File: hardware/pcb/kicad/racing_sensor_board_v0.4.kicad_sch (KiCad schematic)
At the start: 53 parts, among them J0 TC0, J1 TC1, J10 NTC2, J11 NTC3, J12 OUT0, J13 OUT1, J14 OUT2, J15 OUT3, J16 ANA0, J17 ANA1, J18 ANA2, J19 ANA3, J2 TC2, J20 ANA4, J21 ANA5, J22 ANA6, J23 ANA7, J24 DIG0, J25 DIG1, J26 DIG2, J27 DIG3, J28 DIG4, J29 DIG5, J3 TC3, J30 PWR_IN, J4 TC4, J5 TC5, J6 TC6, J7 TC7, J8 NTC0, J9 NTC1, Q1 AO3400A, Q2 AO3400A, Q3 AO3400A, Q4 AO3400A, U1 Teensy_4.1, U10 MAX31855KASA+, U11 LIS3DH, U12 MP2307DN, U2 WIZ820io, U3 MAX31855KASA+, U4 MAX31855KASA+, U5 MAX31855KASA+, U6 MAX31855KASA+, U7 MAX31855KASA+, U8 MAX31855KASA+, U9 MAX31855KASA+

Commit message: Fix unterminated string in v0.4 schematic (MP2307DN note text)
https://claude.ai/code/session_01NVvsy3kMr9piDWfs5WdvpG
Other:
- note added: "Cout, Lout, R-divider — add manually in KiCad"
- note removed: "Cout, Lout, R-divider add manually in KiCad"
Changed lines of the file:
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@@
     (effects (font (size 1.27 1.27)))
  )
-  (text "Cout, Lout, R-divider
-add manually in KiCad" (at 332.00 321.35 0)
+  (text "Cout, Lout, R-divider — add manually in KiCad" (at 332.00 321.35 0)
     (effects (font (size 1.5 1.5)) (justify left))
  )

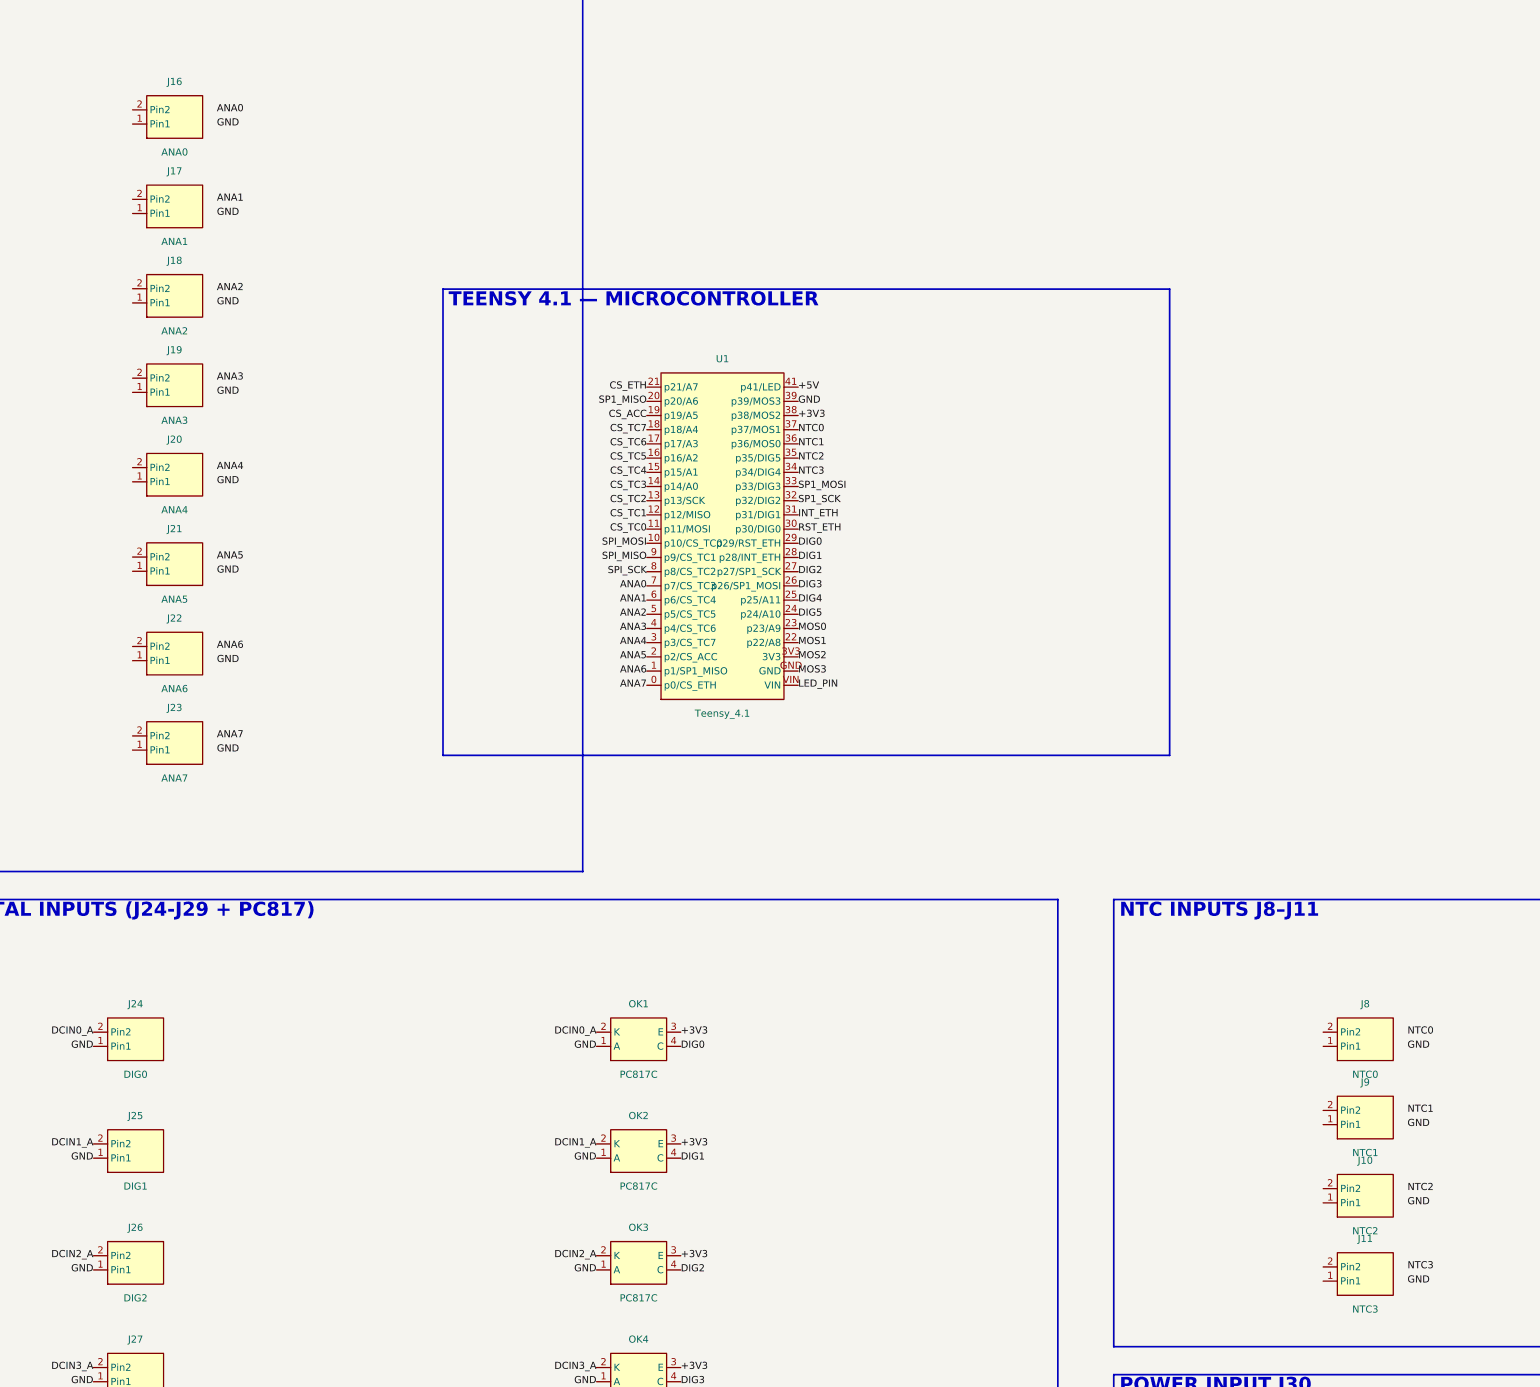
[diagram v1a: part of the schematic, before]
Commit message: Fix pin/label mismatch in v0.4 analog and NTC connector sections
J16-J23 and J8-J11 use Conn2pin which has left-side pins, but labels
were placed on the right side (rp_xy), causing 'Pin not connected' and
'Label not connected' ERC violations. Fixed to use lp_xy/llbl.

https://claude.ai/code/session_01NVvsy3kMr9piDWfs5WdvpG
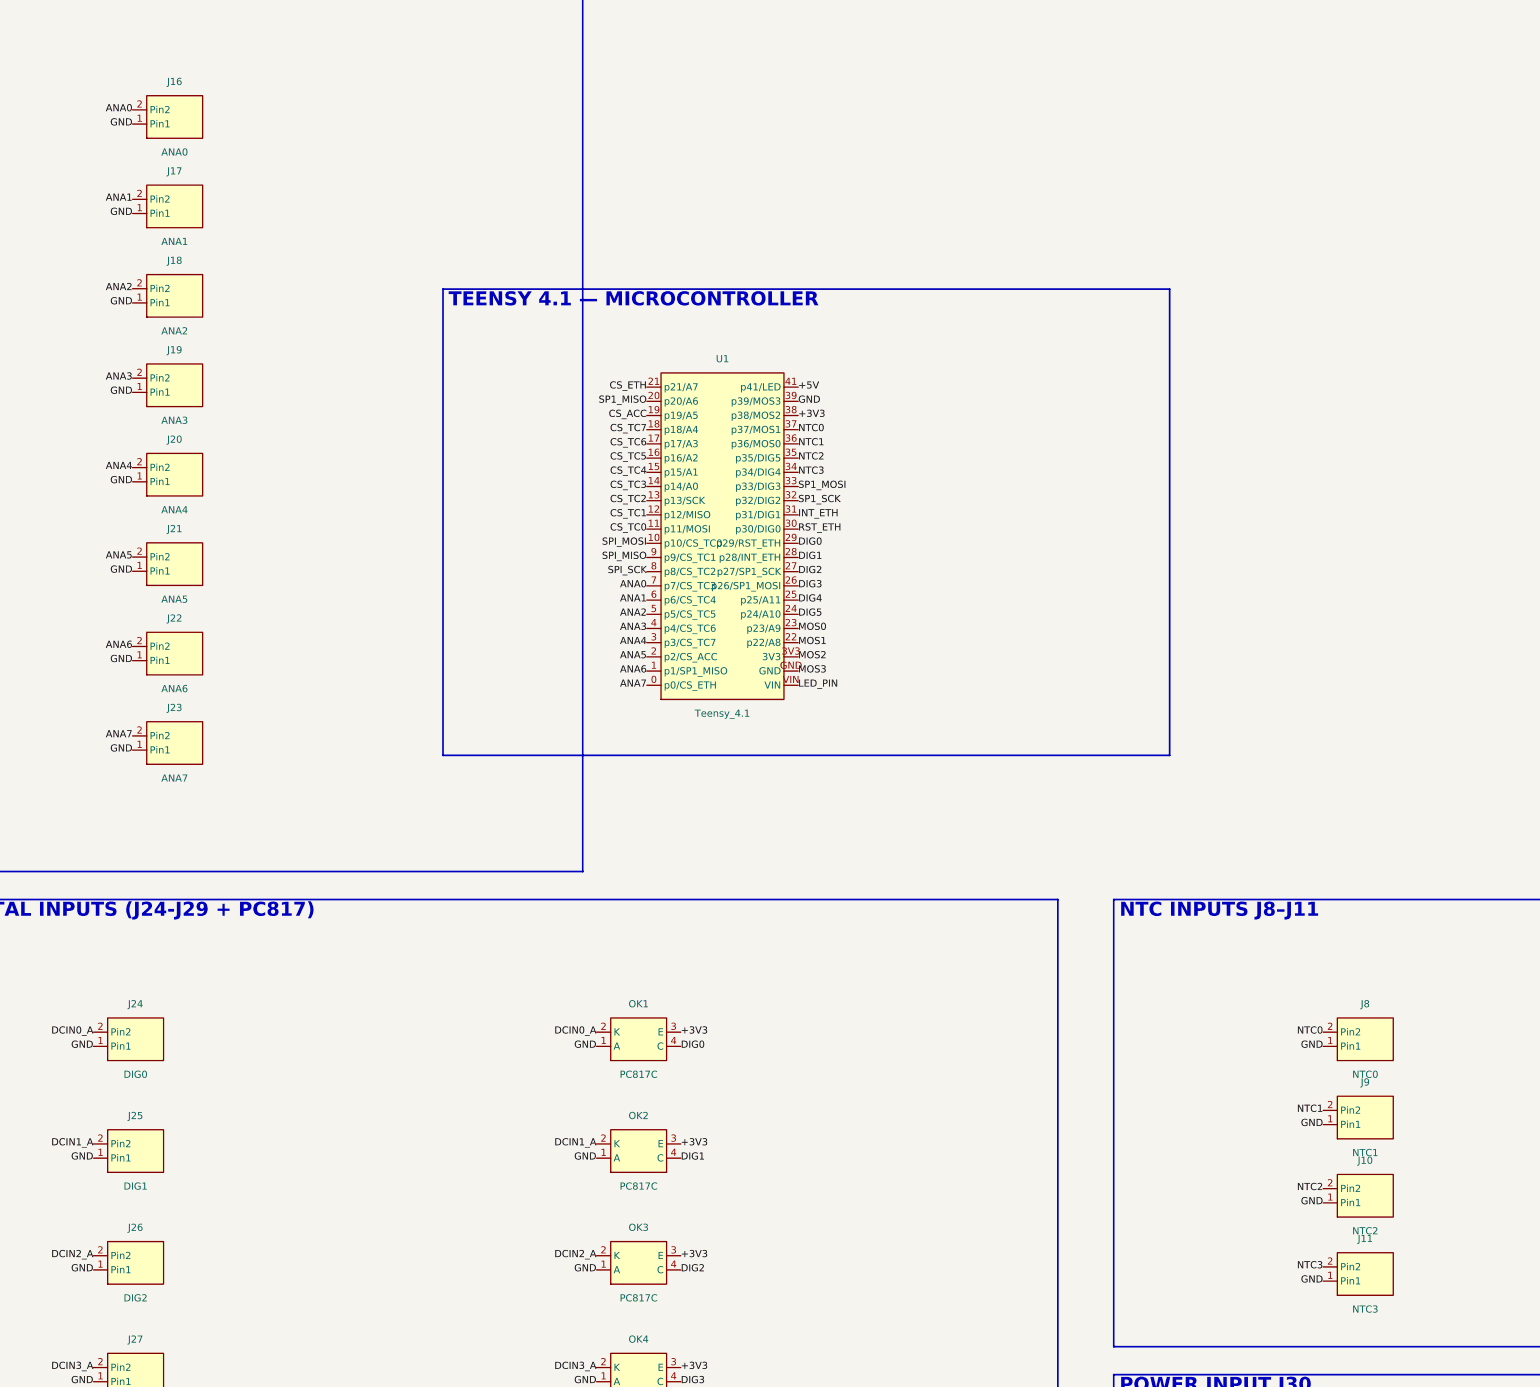
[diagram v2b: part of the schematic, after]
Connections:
- net ANA0: now also J16.2 (Pin2)
- net ANA1: now also J17.2 (Pin2)
- net ANA2: now also J18.2 (Pin2)
- net ANA3: now also J19.2 (Pin2)
- net ANA4: now also J20.2 (Pin2)
- net ANA5: now also J21.2 (Pin2)
- net ANA6: now also J22.2 (Pin2)
- net ANA7: now also J23.2 (Pin2)
- net GND: now also J10.1 (Pin1), J11.1 (Pin1), J16.1 (Pin1), J17.1 (Pin1), J18.1 (Pin1), J19.1 (Pin1), J20.1 (Pin1), J21.1 (Pin1), J22.1 (Pin1), J23.1 (Pin1), J8.1 (Pin1), J9.1 (Pin1)
- net NTC0: now also J8.2 (Pin2)
- net NTC1: now also J9.2 (Pin2)
- net NTC2: now also J10.2 (Pin2)
- net NTC3: now also J11.2 (Pin2)
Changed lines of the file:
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@@
     (pin "2")
   )
-  (label "ANA0" (at 79.54 153.73 0)
-    (effects (font (size 1.27 1.27)))
- )
-  (label "GND" (at 79.54 156.27 0)
+  (label "ANA0" (at 64.46 153.73 180)
+    (effects (font (size 1.27 1.27)))
+ )
+  (label "GND" (at 64.46 156.27 180)
     (effects (font (size 1.27 1.27)))
  )
@@
     (pin "2")
   )
-  (label "ANA1" (at 79.54 169.73 0)
-    (effects (font (size 1.27 1.27)))
- )
-  (label "GND" (at 79.54 172.27 0)
+  (label "ANA1" (at 64.46 169.73 180)
+    (effects (font (size 1.27 1.27)))
+ )
+  (label "GND" (at 64.46 172.27 180)
     (effects (font (size 1.27 1.27)))
  )
@@
     (pin "2")
   )
-  (label "ANA2" (at 79.54 185.73 0)
-    (effects (font (size 1.27 1.27)))
- )
-  (label "GND" (at 79.54 188.27 0)
+  (label "ANA2" (at 64.46 185.73 180)
+    (effects (font (size 1.27 1.27)))
+ )
+  (label "GND" (at 64.46 188.27 180)
     (effects (font (size 1.27 1.27)))
  )
@@
     (pin "2")
   )
-  (label "ANA3" (at 79.54 201.73 0)
-    (effects (font (size 1.27 1.27)))
- )
-  (label "GND" (at 79.54 204.27 0)
+  (label "ANA3" (at 64.46 201.73 180)
+    (effects (font (size 1.27 1.27)))
+ )
+  (label "GND" (at 64.46 204.27 180)
     (effects (font (size 1.27 1.27)))
  )
@@
     (pin "2")
   )
-  (label "ANA4" (at 79.54 217.73 0)
-    (effects (font (size 1.27 1.27)))
- )
-  (label "GND" (at 79.54 220.27 0)
+  (label "ANA4" (at 64.46 217.73 180)
+    (effects (font (size 1.27 1.27)))
+ )
+  (label "GND" (at 64.46 220.27 180)
     (effects (font (size 1.27 1.27)))
  )
@@
     (pin "2")
   )
-  (label "ANA5" (at 79.54 233.73 0)
-    (effects (font (size 1.27 1.27)))
- )
-  (label "GND" (at 79.54 236.27 0)
+  (label "ANA5" (at 64.46 233.73 180)
+    (effects (font (size 1.27 1.27)))
+ )
+  (label "GND" (at 64.46 236.27 180)
     (effects (font (size 1.27 1.27)))
  )
@@
     (pin "2")
   )
-  (label "ANA6" (at 79.54 249.73 0)
-    (effects (font (size 1.27 1.27)))
- )
-  (label "GND" (at 79.54 252.27 0)
+  (label "ANA6" (at 64.46 249.73 180)
+    (effects (font (size 1.27 1.27)))
+ )
+  (label "GND" (at 64.46 252.27 180)
     (effects (font (size 1.27 1.27)))
  )
@@
     (pin "2")
   )
-  (label "ANA7" (at 79.54 265.73 0)
-    (effects (font (size 1.27 1.27)))
- )
-  (label "GND" (at 79.54 268.27 0)
+  (label "ANA7" (at 64.46 265.73 180)
+    (effects (font (size 1.27 1.27)))
+ )
+  (label "GND" (at 64.46 268.27 180)
     (effects (font (size 1.27 1.27)))
  )
@@
     (pin "2")
   )
-  (label "NTC0" (at 292.54 318.73 0)
-    (effects (font (size 1.27 1.27)))
- )
-  (label "GND" (at 292.54 321.27 0)
+  (label "NTC0" (at 277.46 318.73 180)
+    (effects (font (size 1.27 1.27)))
+ )
+  (label "GND" (at 277.46 321.27 180)
     (effects (font (size 1.27 1.27)))
  )
@@
     (pin "2")
   )
-  (label "NTC1" (at 292.54 332.73 0)
-    (effects (font (size 1.27 1.27)))
- )
-  (label "GND" (at 292.54 335.27 0)
+  (label "NTC1" (at 277.46 332.73 180)
+    (effects (font (size 1.27 1.27)))
+ )
+  (label "GND" (at 277.46 335.27 180)
     (effects (font (size 1.27 1.27)))
  )
@@
     (pin "2")
   )
-  (label "NTC2" (at 292.54 346.73 0)
-    (effects (font (size 1.27 1.27)))
- )
-  (label "GND" (at 292.54 349.27 0)
+  (label "NTC2" (at 277.46 346.73 180)
+    (effects (font (size 1.27 1.27)))
+ )
+  (label "GND" (at 277.46 349.27 180)
     (effects (font (size 1.27 1.27)))
  )
@@
     (pin "2")
   )
-  (label "NTC3" (at 292.54 360.73 0)
-    (effects (font (size 1.27 1.27)))
- )
-  (label "GND" (at 292.54 363.27 0)
-    (effects (font (size 1.27 1.27)))
- )
+  (label "NTC3" (at 277.46 360.73 180)
+    (effects (font (size 1.27 1.27)))
+ )
+  (label "GND" (at 277.46 363.27 180)
+    (effects (font (size 1.27 1.27)))
+ )

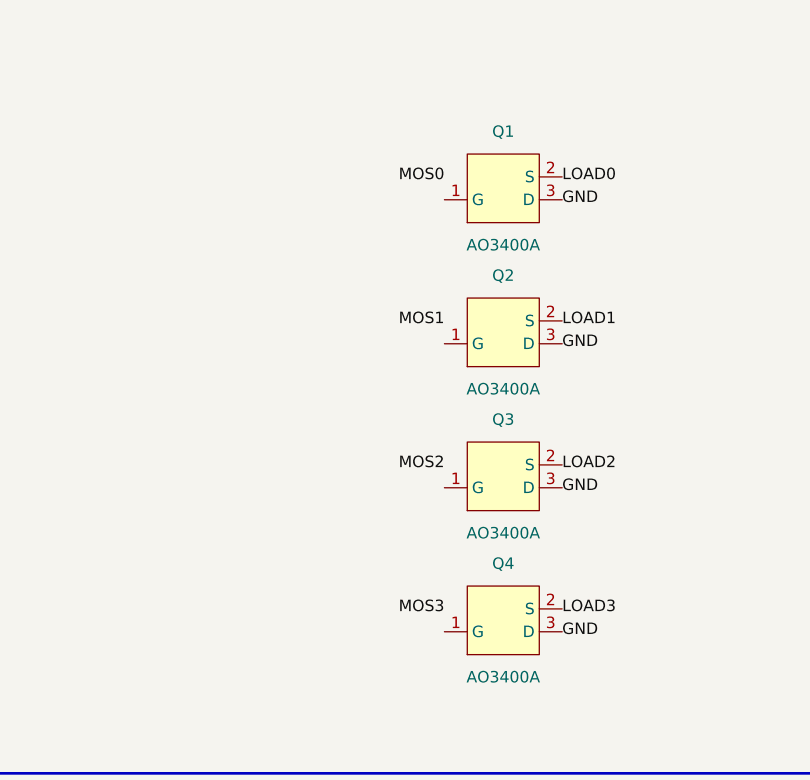
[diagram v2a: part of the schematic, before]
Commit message: Fix remaining 24 ERC errors in KiCad v0.4 schematic
- Add explicit wire stubs (2.54mm) from MOSFET gate pins (Q1-Q4) to
  MOS0-3 net labels — ensures reliable KiCad connectivity detection
- Change all power supply pins (VIN, GND, 3V3, VCC, VDD, VDD_IO) from
  power_in/power_out → passive to eliminate PWR_FLAG ERC errors
- Change MAX31855 SO and LIS3DH SDO from output → passive so the shared
  SPI_MISO bus with 8+ chips doesn't trigger multiple-driver ERC errors
- Change WIZ820io MISO/INTn from output → passive (bus/open-drain)
- Change PC817 A/K from input → passive; E from passive → output so
  the DIG0-5 nets connecting to Teensy input pins have a proper driver

https://claude.ai/code/session_01NVvsy3kMr9piDWfs5WdvpG
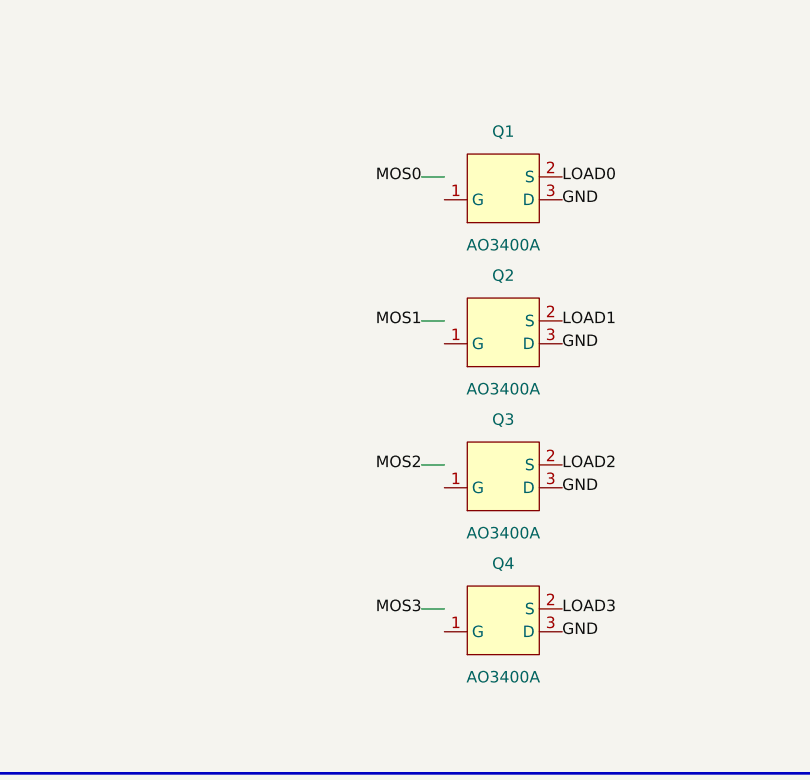
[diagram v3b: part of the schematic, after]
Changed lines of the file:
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@@
     (pin "2")
   )
-  (label "MOS0" (at 83.46 463.73 180)
+  (wire (pts (xy 83.46 463.73) (xy 80.92 463.73))
+    (stroke (width 0) (type default)) )
+  (label "MOS0" (at 80.92 463.73 180)
     (effects (font (size 1.27 1.27)))
  )
@@
     (pin "2")
   )
-  (label "MOS1" (at 83.46 479.73 180)
+  (wire (pts (xy 83.46 479.73) (xy 80.92 479.73))
+    (stroke (width 0) (type default)) )
+  (label "MOS1" (at 80.92 479.73 180)
     (effects (font (size 1.27 1.27)))
  )
@@
     (pin "2")
   )
-  (label "MOS2" (at 83.46 495.73 180)
+  (wire (pts (xy 83.46 495.73) (xy 80.92 495.73))
+    (stroke (width 0) (type default)) )
+  (label "MOS2" (at 80.92 495.73 180)
     (effects (font (size 1.27 1.27)))
  )
@@
     (pin "2")
   )
-  (label "MOS3" (at 83.46 511.73 180)
+  (wire (pts (xy 83.46 511.73) (xy 80.92 511.73))
+    (stroke (width 0) (type default)) )
+  (label "MOS3" (at 80.92 511.73 180)
     (effects (font (size 1.27 1.27)))
  )

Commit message: Fix all ERC errors: snap every pin to 50-mil grid
Root cause: body widths were not multiples of 2.54 mm, so hw was not
a multiple of 1.27 mm, making every pin endpoint land off the KiCad
50-mil grid. KiCad refuses to connect labels/wires to off-grid pins,
so virtually all net connections were silently broken.

Changes:
- All bw values rounded up to nearest multiple of 2.54 mm (4*2.54 to
  9*2.54) so hw = k*1.27 mm for integer k
- All instance positions (cx, cy) passed through gp() which snaps to
  the nearest multiple of 1.27 mm
- All loop offsets (row/col spacing) also snapped via gp()
- Added grid-verification pass at generator end that checks every
  lib-symbol pin 'at' coordinate is within 0.005 mm of a grid point
- MP2307DN EN/FB changed input->passive (no external driver on those
  single-connection nets, avoids ERC 'input not driven' errors)
- PC817 E remains 'output' to drive DIG0-5 nets to Teensy inputs
- MOSFET gate wire stubs retained (belt-and-suspenders for gates)
- lp_xy/rp_xy formula updated to use 2*G constant (cleaner, same math)

https://claude.ai/code/session_01NVvsy3kMr9piDWfs5WdvpG
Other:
- note added: "0-5V sensors → Teensy A0-A7 (p14-21)"
- note added: "ANA0-7:"
- note added: "ANALOG IN J16-J23"
- note added: "CS_TC0-7:"
- note added: "DIG0-5:"
- note added: "MOS0-3:"
- note added: "MP2307DN output 12V → 5V"
- note added: "NTC INPUTS J8-J11"
- note added: "NTC pull-up → Teensy A8-A11 (p22-25)"
- note added: "NTC0-3:"
- note added: "PC817 out → Teensy p30-35"
- note added: "TC0-7 +/-:"
- note added: "Teensy p10,9,8,7,6,5,4,3 → MAX31855"
- note added: "Teensy p11/12/13 → MAX31855 ×8 + LIS3DH"
- note added: "Teensy p36-39 → R → MOSFET gate"
- note added: "Teensy regulator max 250mA"
- note added: "Thermocouple T+/T- → MAX31855"
- note added: "Vehicle supply 10-16V"
- note removed: "0–5V sensors → Teensy A0–A7 (p14–21)"
- note removed: "ANA0–7:"
- note removed: "ANALOG IN J16–J23"
- note removed: "CS_TC0–7:"
- note removed: "DIG0–5:"
- note removed: "MOS0–3:"
- note removed: "MP2307DN output (12V → 5V)"
- note removed: "NTC INPUTS J8–J11"
- note removed: "NTC pull-up → Teensy A8–A11 (p22–25)"
- note removed: "NTC0–3:"
- note removed: "PC817 out → Teensy p30–35"
- note removed: "TC0–7 +/-:"
- note removed: "Teensy onboard regulator (max 250mA)"
- note removed: "Teensy p10,9,8,7,6,5,4,3 → MAX31855 U3–U10"
- note removed: "Teensy p11/12/13 → all MAX31855 + LIS3DH"
- note removed: "Teensy p36–39 → R → MOSFET gate"
- note removed: "Thermocouple T+/T- → MAX31855 inputs"
- note removed: "Vehicle supply (10–16V)"
